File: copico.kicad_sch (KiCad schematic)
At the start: 30 parts, among them P1 CocoEdgeConnector, P10 Power Bus, P2 5V Data Bus, P3 3.3V Data Bus, P4 5V Address Bus, P5 3.3V Address Bus, U1 74LS133, U2 74LS06, U3 PicoW, U4 SN74LVC245A, U5 SN74LVC245A, U6 SN74LVC245A, U7 SN74LVC4245A, U8 SN74LVC245A

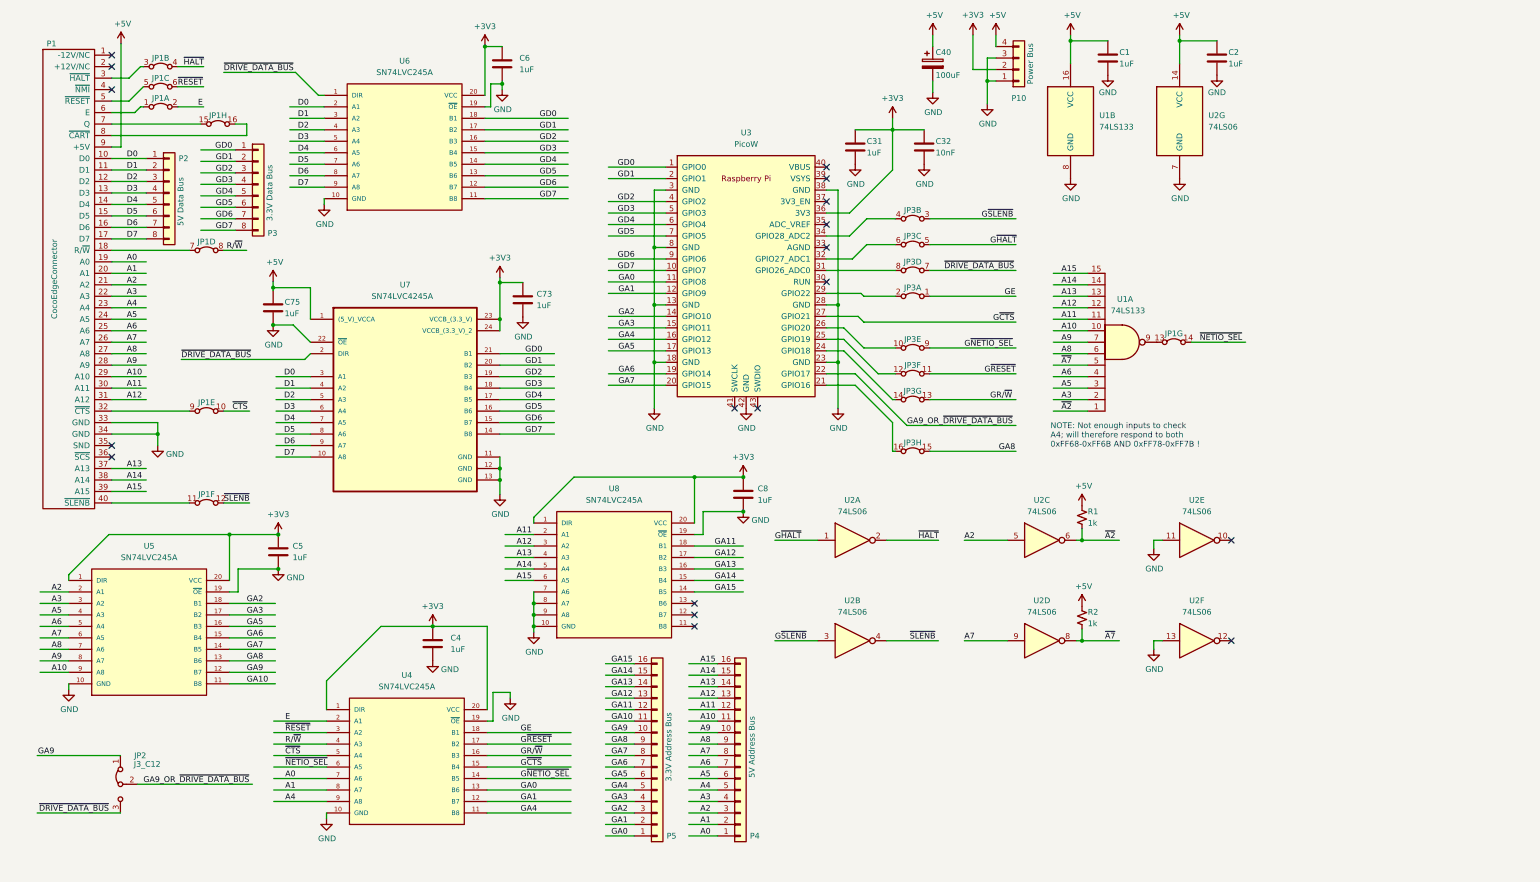
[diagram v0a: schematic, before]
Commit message: Correct signal naming on schematic & URL on PCB
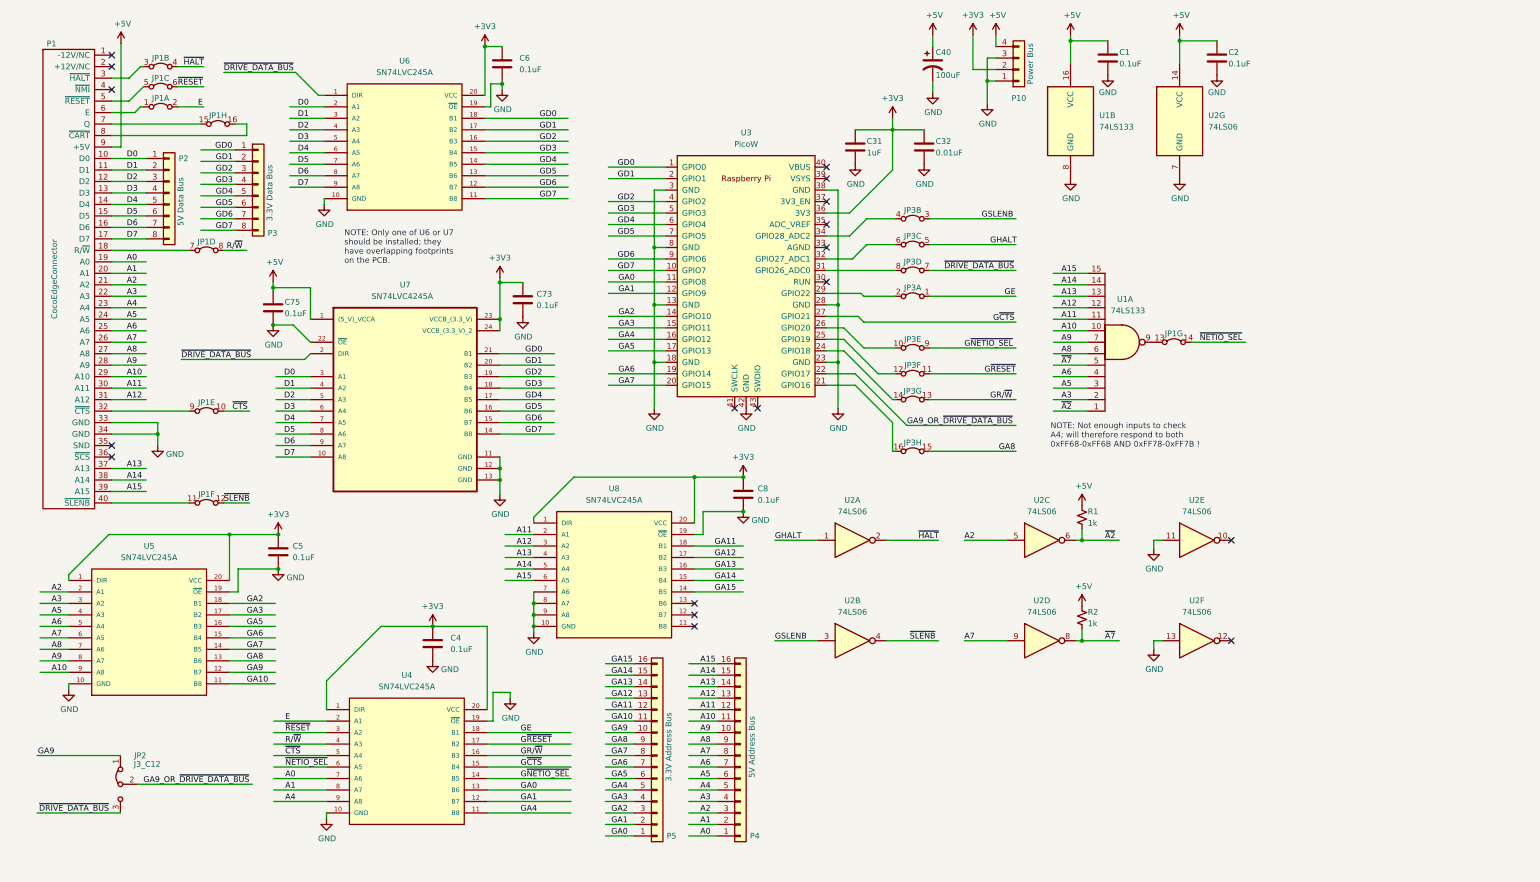
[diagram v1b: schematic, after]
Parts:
- C1, C2, C4, C5, C6, C73, C75, C8: value 1uF -> 0.1uF
- C32: value 10nF -> 0.01uF
- C40: symbol PCM_Capacitor_AKL:CP_Generic -> Device:C_Polarized_US
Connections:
- net G~{HALT} renamed GHALT
- net G~{SLENB} renamed GSLENB
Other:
- note added: "NOTE: Only one of U6 or U7 should be installed; they have overlapping footprints on the PCB."
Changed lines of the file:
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@@
   (title_block
     (title "CoPiCo: WiFi and more for the Tandy Color Computer")
-    (date "2024-02-06")
-    (rev "0.8.0")
+    (date "2024-02-18")
+    (rev "0.1.10")
     (company "Thomas Shanks (copico@tshanks.org)")
-    (comment 1 "https://github.com/JayesonLS/TandyCircuitsAndLogic/tree/master/CoCoProtoBoard")
-    (comment 2 "Board footprint based on the Public Domain CoCoProtoBoard:")
-    (comment 4 "https://github.com/thomasshanks/copico-board")
+    (comment 1 "found at: github.com/JayesonLS/TandyCircuitsAndLogic/tree/master/CoCoProtoBoard")
+    (comment 2 "Board footprint based on the Public Domain CoCoProtoBoard, which can be")
+    (comment 3 "Released under the MIT License (opensource.org/license/mit)")
+    (comment 4 "GitHub Repo: https://github.com/thomasshanks/copico-board")
   )
   (junction (at 150.495 65.405) (diameter 0) (color 0 0 0 0)
@@
     (effects (font (size 1.27 1.27)) (justify left bottom))
   )
+  (text "NOTE: Only one of U6 or U7\nshould be installed; they\nhave overlapping footprints\non the PCB."
+    (at 81.915 69.215 0)
+    (effects (font (size 1.27 1.27)) (justify left bottom))
+  )
   (label "~{DRIVE_DATA_BUS}" (at 29.845 190.5 180) (fields_autoplaced)
     (effects (font (size 1.27 1.27)) (justify right bottom))
@@
     (effects (font (size 1.27 1.27)) (justify left bottom))
   )
-  (label "G~{SLENB}" (at 177.165 152.4 0) (fields_autoplaced)
+  (label "GSLENB" (at 177.165 152.4 0) (fields_autoplaced)
     (effects (font (size 1.27 1.27)) (justify left bottom))
   )
@@
     (effects (font (size 1.27 1.27)) (justify left bottom))
   )
-  (label "G~{SLENB}" (at 222.885 59.055 0) (fields_autoplaced)
+  (label "GSLENB" (at 222.885 59.055 0) (fields_autoplaced)
     (effects (font (size 1.27 1.27)) (justify left bottom))
   )
@@
     (effects (font (size 1.27 1.27)) (justify left bottom))
   )
-  (label "G~{HALT}" (at 177.165 130.175 0) (fields_autoplaced)
+  (label "GHALT" (at 177.165 130.175 0) (fields_autoplaced)
     (effects (font (size 1.27 1.27)) (justify left bottom))
   )
@@
     (effects (font (size 1.27 1.27)) (justify left bottom))
   )
-  (label "G~{HALT}" (at 224.79 64.77 0) (fields_autoplaced)
+  (label "GHALT" (at 224.79 64.77 0) (fields_autoplaced)
     (effects (font (size 1.27 1.27)) (justify left bottom))
   )
@@
     (effects (font (size 1.27 1.27)) (justify left bottom))
   )
-  (symbol (lib_id "PCM_Capacitor_AKL:CP_Generic") (at 212.09 24.765 0) (unit 1)
+  (symbol (lib_id "Device:C_Polarized_US") (at 212.09 24.765 0) (unit 1)
     (in_bom yes) (on_board yes) (dnp no)
     (property "Reference" "C40" (at 212.725 22.225 0)
@@
       (effects (font (size 1.27 1.27)) (justify left))
     )
-    (property "Footprint" "Capacitor_THT:CP_Radial_D7.5mm_P2.50mm" (at 213.0552 28.575 0)
+    (property "Footprint" "Capacitor_THT:CP_Radial_D7.5mm_P2.50mm" (at 212.09 24.765 0)
       (effects (font (size 1.27 1.27)) hide)
     )
@@
       (effects (font (size 1.27 1.27)) (justify left))
     )
-    (property "Value" "10nF" (at 212.725 44.45 0)
+    (property "Value" "0.01uF" (at 212.725 44.45 0)
       (effects (font (size 1.27 1.27)) (justify left))
     )
@@
       (effects (font (size 1.27 1.27)) (justify left))
     )
-    (property "Value" "1uF" (at 253.365 24.765 0)
+    (property "Value" "0.1uF" (at 253.365 24.765 0)
       (effects (font (size 1.27 1.27)) (justify left))
     )
@@
       (effects (font (size 1.27 1.27)) (justify left))
     )
-    (property "Value" "1uF" (at 277.495 24.765 0)
+    (property "Value" "0.1uF" (at 277.495 24.765 0)
       (effects (font (size 1.27 1.27)) (justify left))
     )
@@
       (effects (font (size 1.27 1.27)) (justify left))
     )
-    (property "Value" "1uF" (at 70.485 133.985 0)
+    (property "Value" "0.1uF" (at 70.485 133.985 0)
       (effects (font (size 1.27 1.27)) (justify left))
     )
@@
       (effects (font (size 1.27 1.27)) (justify left))
     )
-    (property "Value" "1uF" (at 120.65 26.035 0)
+    (property "Value" "0.1uF" (at 120.65 26.035 0)
       (effects (font (size 1.27 1.27)) (justify left))
     )
@@
       (effects (font (size 1.27 1.27)) (justify left))
     )
-    (property "Value" "1uF" (at 124.46 78.232 0)
+    (property "Value" "0.1uF" (at 124.46 78.232 0)
       (effects (font (size 1.27 1.27)) (justify left))
     )
@@
       (effects (font (size 1.27 1.27)) (justify left))
     )
-    (property "Value" "1uF" (at 68.707 80.01 0)
+    (property "Value" "0.1uF" (at 68.707 80.01 0)
       (effects (font (size 1.27 1.27)) (justify left))
     )
@@
       (effects (font (size 1.27 1.27)) (justify left))
     )
-    (property "Value" "1uF" (at 105.41 154.305 0)
+    (property "Value" "0.1uF" (at 105.41 154.305 0)
       (effects (font (size 1.27 1.27)) (justify left))
     )
@@
       (effects (font (size 1.27 1.27)) (justify left))
     )
-    (property "Value" "1uF" (at 173.355 121.285 0)
+    (property "Value" "0.1uF" (at 173.355 121.285 0)
       (effects (font (size 1.27 1.27)) (justify left))
     )

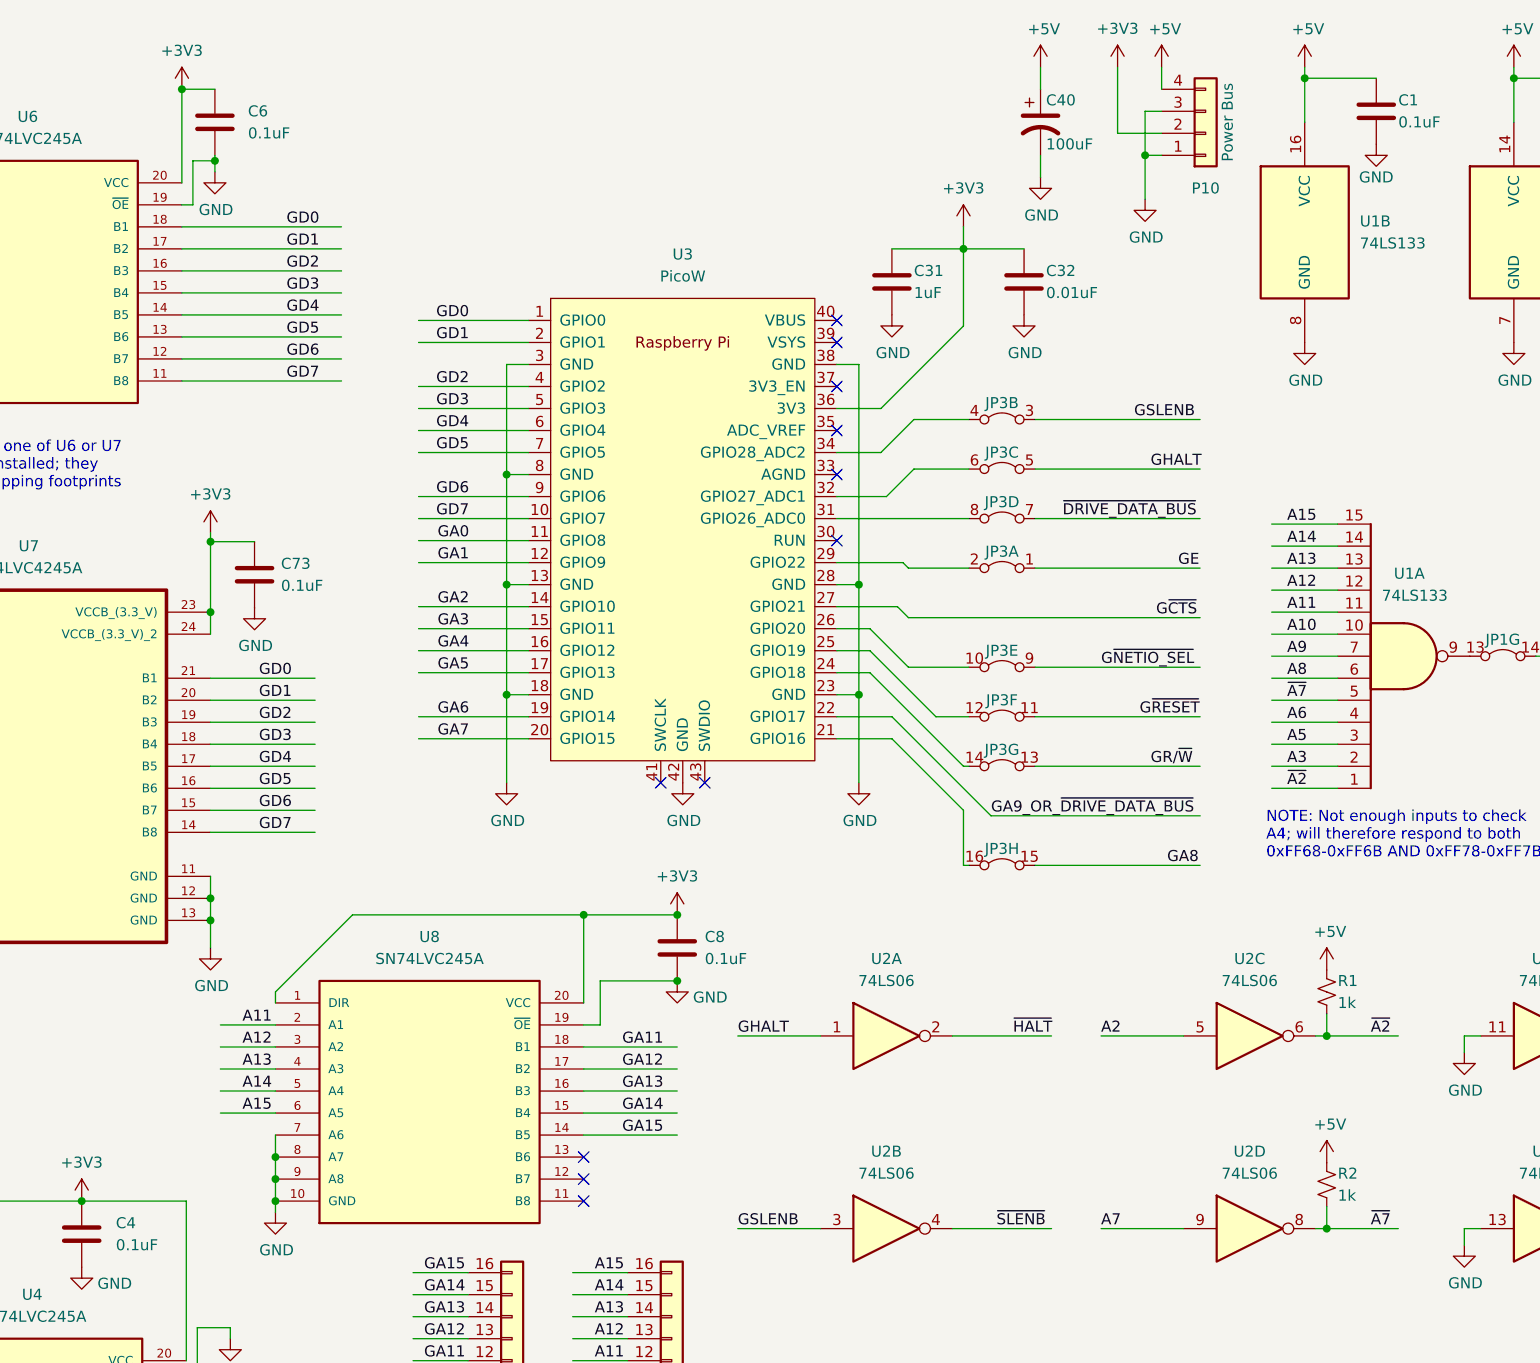
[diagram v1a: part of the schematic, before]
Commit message: Update component values to match reality
- Update component values to match what we actually used on the board.

- Add an additional decoupling capacitor for the PicoW to the schematic. This
  capacitor is not yet laid out onto the actual board.

- Take the bar off of the GHALT and GSLENB signals since they are actually
  active high, not active low.

- Additional schematic cleanup.
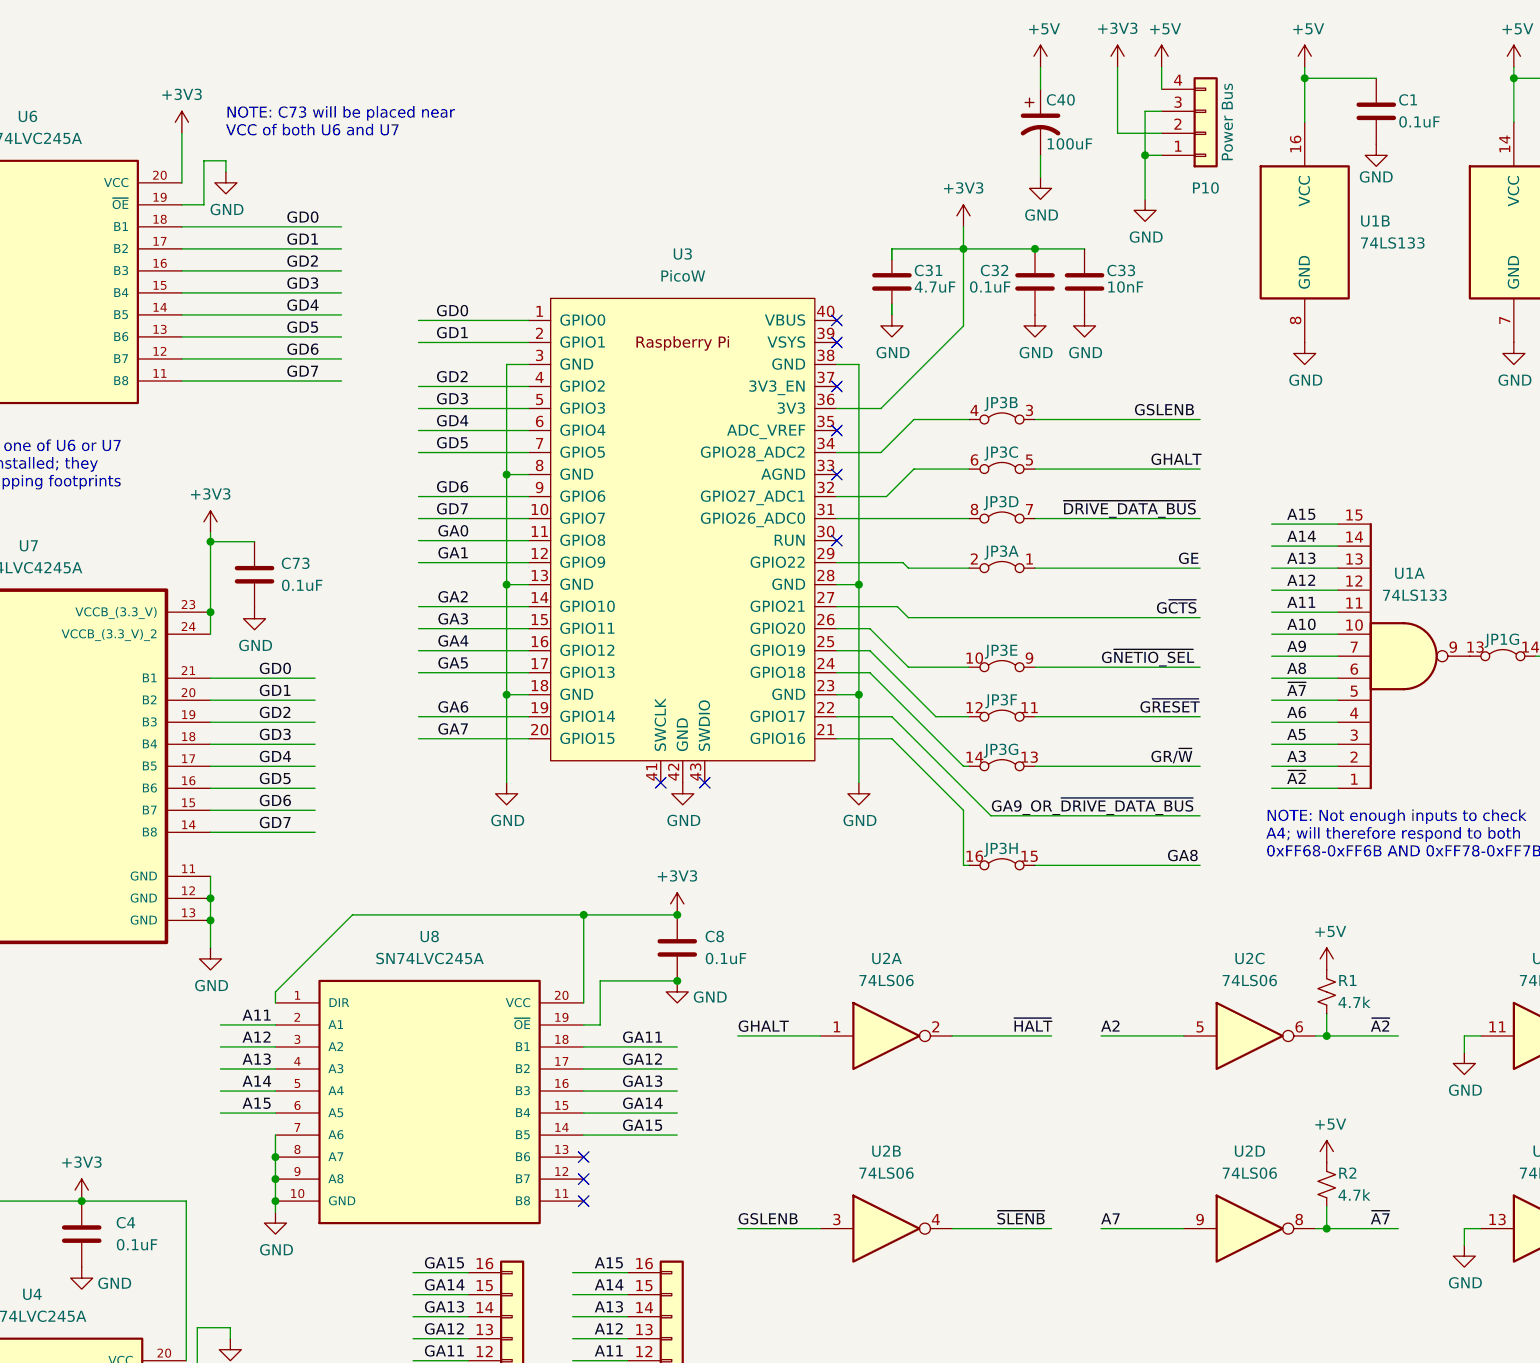
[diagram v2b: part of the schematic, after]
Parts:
- removed C6: 0.1uF, 00_Custom:C_Disc_D5.0mm_W2.5mm_P200mils, symbol Device:C
- added C33: 10nF, Capacitor_THT:C_Disc_D5.0mm_W2.5mm_P5.00mm, symbol Device:C
- C31: value 1uF -> 4.7uF; footprint Capacitor_THT:C_Disc_D5.0mm_W2.5mm_P5.00mm -> PCM_Capacitor_THT_US_AKL:CP_Radial_Tantal_D4.5mm_P5.00mm
- C32: value 0.01uF -> 0.1uF
- R1, R2: value 1k -> 4.7k
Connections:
- net +3V3: now also C33.1
- net GND: now also C33.2
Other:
- note added: "NOTE: C73 will be placed near VCC of both U6 and U7"
- moved on the sheet: C32
